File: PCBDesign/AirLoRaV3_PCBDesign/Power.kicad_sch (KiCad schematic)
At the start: 16 parts, among them J1 Barrel_Jack_Switch_Pin3Ring, U1 TPS7A2633DRVR, U4 TPS54202DDC

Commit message: Update circiut
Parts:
- added C3: 75pF, Capacitor_SMD:C_0603_1608Metric, symbol Device:C_Small
- added C5: 22uF, Capacitor_SMD:C_0603_1608Metric, symbol Device:C_Small
- added R1: 100K, Resistor_SMD:R_0603_1608Metric, symbol Device:R
- C1: value 470uF -> 10uF
- C2: renamed from C14; value 470uF -> 0.1uF; footprint Capacitor_Tantalum_SMD:CP_EIA-7343-43_Kemet-X -> Capacitor_SMD:C_0603_1608Metric
- C4: renamed from C15; value 100Uf -> 0.1uF; footprint Capacitor_Tantalum_SMD:CP_EIA-6032-15_Kemet-U -> Capacitor_SMD:C_0603_1608Metric
- C6: renamed from C2; value 100Uf -> 22uF; footprint Capacitor_Tantalum_SMD:CP_EIA-6032-15_Kemet-U -> Capacitor_SMD:C_0603_1608Metric
- C7: renamed from C3; footprint (none) -> Capacitor_SMD:C_0603_1608Metric
- C8: renamed from C5; footprint (none) -> Capacitor_SMD:C_0603_1608Metric
- L1: value 68uH -> 15uH
- R2: renamed from R7; value R -> 13.3K; footprint (none) -> Resistor_SMD:R_0603_1608Metric
- R3: renamed from R6; value R -> 49.9; footprint (none) -> Resistor_SMD:R_0603_1608Metric
- R4: renamed from R10; value R -> 10K; footprint (none) -> Resistor_SMD:R_0603_1608Metric
- R5: renamed from R8; value R -> 1.96M; footprint (none) -> Resistor_SMD:R_0603_1608Metric
- R6: renamed from R9; value R -> 1.18M; footprint (none) -> Resistor_SMD:R_0603_1608Metric
- U1: renamed from U4; LCSC (none) -> C191884; MFR (none) -> TPS54202DDCR
- U2: renamed from U1; footprint TPS7A2633DRVR:SON65P200X200X80-7N -> footprint:TPS7A2633DRVR; LCSC (none) -> C2876256; MFR (none) -> TPS7A2633DRVR
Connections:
- net GND: now also U2.7 (EXP), C5.2
- net at C4.2, L1.1, U1.2 (SW): no longer R3.1
- net at R2.1, U1.4 (FB): now also C3.2, R1.2; no longer R3.2
- net 3.3V renamed +3.3V
- net 5V renamed +5V
- net +5V: now also R3.2, C5.1
- new net: C3.1, R1.1, R3.1
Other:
- moved on the sheet: C1, C2, C4, C6, C7, C8, D1, J1, L1, R2, R3, R4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

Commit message: Update PCB layout
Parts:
- removed J1: Barrel_Jack_Switch_Pin3Ring, Connector_BarrelJack:BarrelJack_Wuerth_6941xx301002, symbol Connector:Barrel_Jack_Switch_Pin3Ring
- added D2, D3: LED, LED_SMD:LED_0603_1608Metric_Pad1.05x0.95mm_HandSolder, symbol Device:LED
- added J1: 12V, Connector_Phoenix_MC:PhoenixContact_MCV_1,5_2-G-3.5_1x02_P3.50mm_Vertical, symbol Connector:Screw_Terminal_01x02
- added R1, R5, R9: 1k, Resistor_SMD:R_0603_1608Metric, symbol Device:R
- C1: footprint Capacitor_Tantalum_SMD:CP_EIA-7343-43_Kemet-X -> Capacitor_SMD:C_1206_3216Metric_Pad1.33x1.80mm_HandSolder
- C5, C7, C8: footprint Capacitor_SMD:C_0603_1608Metric -> Capacitor_SMD:C_1206_3216Metric_Pad1.33x1.80mm_HandSolder
- L1: footprint Inductor_SMD:L_Bourns_SRP7028A_7.3x6.6mm -> Inductor_SMD:L_Vishay_IHLP-2020
- renumbered R1 to R2, R2 to R3, R3 to R4, R4 to R6, R5 to R7, R6 to R8
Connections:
- net +3.3V: now also D3.2 (A)
- net +5V: now also D2.2 (A)
- net En: now also R1.2; no longer U1.5 (EN)
- net GND: now also J1.2 (Pin_2), R5.2, R9.2
- net at D1.2 (A): now also J1.1 (Pin_1)
- net SW: now reaches C4.2, L1.1, U1.2 (SW)
- new net: D2.1 (K), R5.1
- new net: D3.1 (K), R9.1
- new net: R1.1, U1.5 (EN)

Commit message: update
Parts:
- C6: footprint Capacitor_SMD:C_0603_1608Metric -> Capacitor_SMD:C_1206_3216Metric_Pad1.33x1.80mm_HandSolder
- C7, C8: footprint Capacitor_SMD:C_1206_3216Metric_Pad1.33x1.80mm_HandSolder -> Capacitor_SMD:C_0805_2012Metric_Pad1.18x1.45mm_HandSolder

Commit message: Update schematic
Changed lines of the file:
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@@
 	(wire
 		(pts
-			(xy 57.15 87.63) (xy 57.15 80.01)
+			(xy 54.61 80.01) (xy 54.61 83.82)
 		)
 		(stroke
@@
 	(wire
 		(pts
-			(xy 54.61 80.01) (xy 57.15 80.01)
-		)
-		(stroke
-			(width 0)
-			(type default)
-		)
-	)
-	(wire
-		(pts
 			(xy 190.5 85.09) (xy 190.5 80.01)
 		)
@@
 	(wire
 		(pts
+			(xy 54.61 83.82) (xy 57.15 83.82)
+		)
+		(stroke
+			(width 0)
+			(type default)
+		)
+	)
+	(wire
+		(pts
 			(xy 121.92 87.63) (xy 125.73 87.63)
 		)
@@
 		)
 		(stroke
+			(width 0)
+			(type default)
+		)
+	)
+	(wire
+		(pts
+			(xy 57.15 83.82) (xy 57.15 87.63)
+		)
+		(stroke

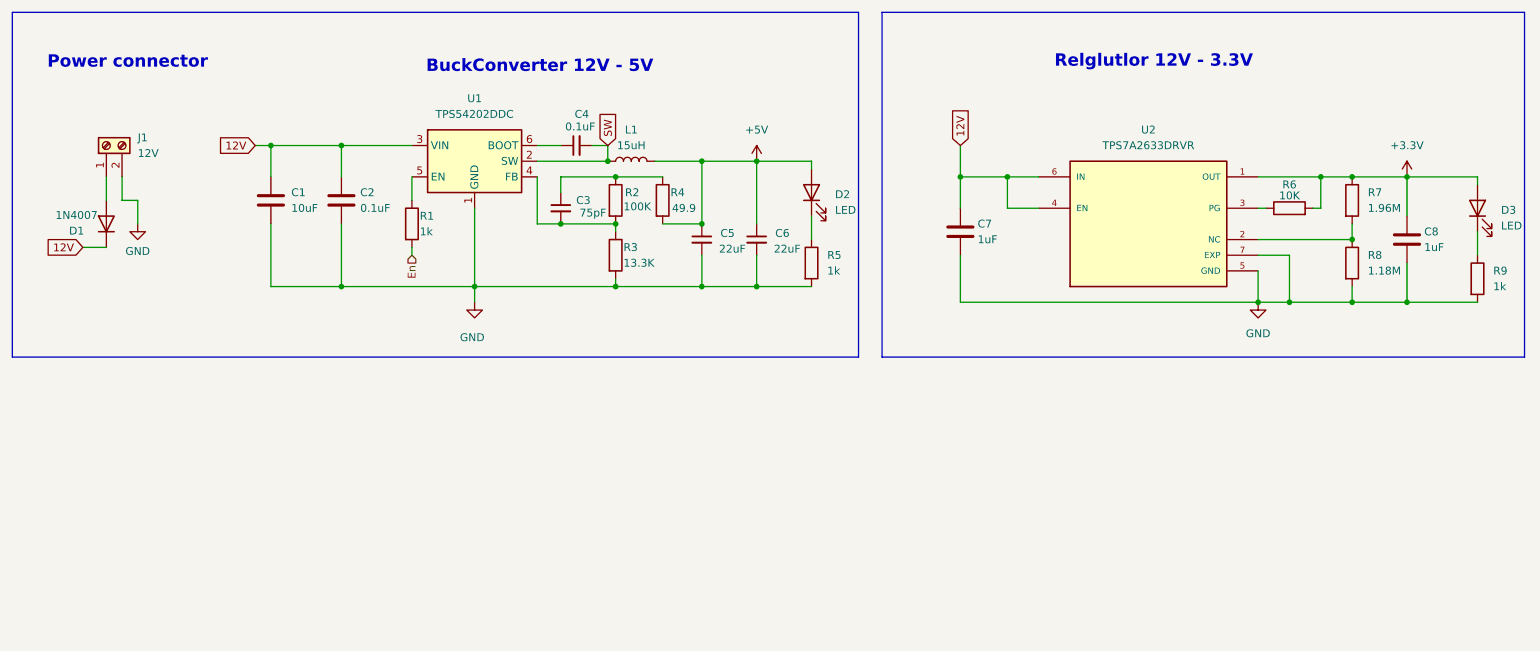
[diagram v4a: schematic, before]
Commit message: Update circuit buck converter and sensor
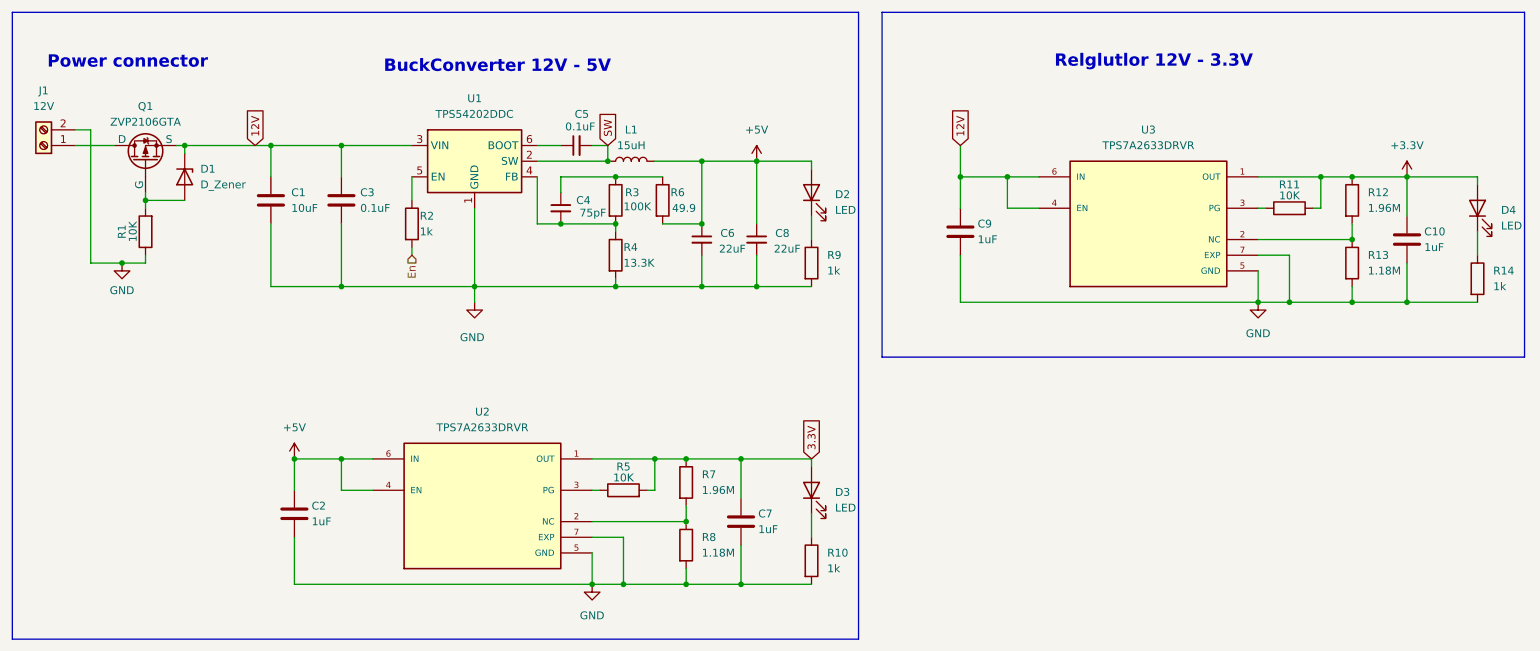
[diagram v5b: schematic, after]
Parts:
- removed D1: 1N4007, Diode_SMD:D_SMA, symbol Device:D
- added C2, C7: 1uF, Capacitor_SMD:C_0805_2012Metric_Pad1.18x1.45mm_HandSolder, symbol Device:C
- added D1: D_Zener, Diode_SMD:D_SMA_Handsoldering, symbol Device:D_Zener
- added D3: LED, LED_SMD:LED_0603_1608Metric_Pad1.05x0.95mm_HandSolder, symbol Device:LED
- added Q1: ZVP2106GTA, Package_TO_SOT_SMD:SOT-223-3_TabPin2, symbol Simulation_SPICE:PMOS
- added R1, R5: 10K, Resistor_SMD:R_0603_1608Metric, symbol Device:R
- added R10: 1k, Resistor_SMD:R_0603_1608Metric, symbol Device:R
- added R7: 1.96M, Resistor_SMD:R_0603_1608Metric, symbol Device:R
- added R8: 1.18M, Resistor_SMD:R_0603_1608Metric, symbol Device:R
- added U2: TPS7A2633DRVR, footprint:TPS7A2633DRVR, symbol TPS7A2633DRVR:TPS7A2633DRVR
- renumbered C8 to C10, C2 to C3, C3 to C4, C4 to C5, C5 to C6, C6 to C8, C7 to C9, D3 to D4, R6 to R11, R7 to R12, R8 to R13, R9 to R14, R1 to R2, R2 to R3, R3 to R4, R4 to R6, R5 to R9, U2 to U3
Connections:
- net +5V: now also C2.1, U2.4 (EN), U2.6 (IN)
- net 12V: now also D1.1 (K), Q1.3 (S)
- net GND: now also C2.2, C7.2, R1.1, R10.2, R8.2, U2.5 (GND), U2.7 (EXP)
- net at J1.1 (Pin_1): now also Q1.2 (D)
- new net: D3.1 (K), R10.1
- new net: R7.2, R8.1, U2.2 (NC)
- new net: D1.2 (A), Q1.1 (G), R1.2
- new net: R5.1, U2.3 (PG)
- new net 3.3V: C7.1, D3.2 (A), R5.2, R7.1, U2.1 (OUT)
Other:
- moved on the sheet: J1

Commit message: Update schematic
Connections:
- net 12V renamed +12V
- net 3.3V renamed +3.3V_HP
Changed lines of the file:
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@@
 	)
 	(junction
+		(at 190.5 80.01)
+		(diameter 0)
+		(color 0 0 0 0)
+	)
+	(junction
 		(at 90.17 74.93)
 		(diameter 0)
@@
 	)
 	(junction
-		(at 190.5 80.01)
+		(at 166.37 125.73)
 		(diameter 0)
 		(color 0 0 0 0)
@@
 	(wire
 		(pts
-			(xy 190.5 80.01) (xy 190.5 74.93)
-		)
-		(stroke
-			(width 0)
-			(type default)
-		)
-	)
-	(wire
-		(pts
 			(xy 101.6 83.82) (xy 101.6 80.01)
 		)
@@
 		)
 	)
-	(global_label "3.3V"
-		(shape input)
-		(at 166.37 125.73 90)
-		(fields_autoplaced yes)
-		(effects
-			(font
-				(size 1.27 1.27)
-			)
-			(justify left)
-		)
-		(property "Intersheetrefs" "${INTERSHEET_REFS}"
-			(at 166.37 118.6324 90)
-			(effects
-				(font
-					(size 1.27 1.27)
-				)
-				(justify left)
-				(hide yes)
-			)
-		)
-	)
-	(global_label "12V"
-		(shape input)
-		(at 190.5 74.93 90)
-		(fields_autoplaced yes)
-		(effects
-			(font
-				(size 1.27 1.27)
-			)
-			(justify left)
-		)
-		(property "Intersheetrefs" "${INTERSHEET_REFS}"
-			(at 190.5 68.4372 90)
-			(effects
-				(font
-					(size 1.27 1.27)
-				)
-				(justify left)
-				(hide yes)
-			)
-		)
-	)
 	(global_label "SW"
 		(shape input)
@@
 		)
 	)
-	(global_label "12V"
-		(shape input)
-		(at 76.2 74.93 90)
-		(fields_autoplaced yes)
-		(effects
-			(font
-				(size 1.27 1.27)
-			)
-			(justify left)
-		)
-		(property "Intersheetrefs" "${INTERSHEET_REFS}"
-			(at 76.2 68.4372 90)
-			(effects
-				(font
-					(size 1.27 1.27)
-				)
-				(justify left)
-				(hide yes)
-			)
-		)
-	)
 	(hierarchical_label "En"
 		(shape input)
@@
 	)
 	(symbol
+		(lib_id "power:+3.3V")
+		(at 166.37 125.73 0)
+		(unit 1)
+		(exclude_from_sim no)
+		(in_bom yes)
+		(on_board yes)
+		(dnp no)
+		(fields_autoplaced yes)
+		(property "Reference" "#PWR067"
+			(at 166.37 129.54 0)
+			(effects
+				(font
+					(size 1.27 1.27)
+				)
+				(hide yes)
+			)
+		)
+		(property "Value" "+3.3V_HP"
+			(at 166.37 120.65 0)
+			(effects
+				(font
+					(size 1.27 1.27)
+				)
+			)
+		)
+		(property "Footprint" ""
+			(at 166.37 125.73 0)
+			(effects
+				(font
+					(size 1.27 1.27)
+				)
+				(hide yes)
+			)
+		)
+		(property "Datasheet" ""
+			(at 166.37 125.73 0)
+			(effects
+				(font
+					(size 1.27 1.27)
+				)
+				(hide yes)
+			)
+		)
+		(property "Description" "Power symbol creates a global label with name \"+3.3V\""
+			(at 166.37 125.73 0)
+			(effects
+				(font
+					(size 1.27 1.27)
+				)
+				(hide yes)
+			)
+		)
+		(pin "1"
+		)
+		(instances
+			(project "airlora-kicad"
+				(path "/59d971df-d6c1-4ef7-a085-bf08b7b16047/be77b740-d58b-414b-97ce-61f1d1685314/af8bb3f5-67b6-4471-83fd-9297b14489a9"
+					(reference "#PWR067")
+					(unit 1)
+				)
+			)
+		)
+	)
+	(symbol
 		(lib_id "Device:R")
 		(at 254 83.82 0)
@@
 	)
 	(symbol
+		(lib_id "power:+12V")
+		(at 78.74 74.93 0)
+		(unit 1)
+		(exclude_from_sim no)
+		(in_bom yes)
+		(on_board yes)
+		(dnp no)
+		(fields_autoplaced yes)
+		(property "Reference" "#PWR065"
+			(at 78.74 78.74 0)
+			(effects
+				(font
+					(size 1.27 1.27)
+				)
+				(hide yes)
+			)
+		)
+		(property "Value" "+12V"
+			(at 78.74 69.85 0)
+			(effects
+				(font
+					(size 1.27 1.27)
+				)
+			)
+		)
+		(property "Footprint" ""
+			(at 78.74 74.93 0)
+			(effects
+				(font
+					(size 1.27 1.27)
+				)
+				(hide yes)
+			)
+		)
+		(property "Datasheet" ""
+			(at 78.74 74.93 0)
+			(effects
+				(font
+					(size 1.27 1.27)
+				)
+				(hide yes)
+			)
+		)
+		(property "Description" "Power symbol creates a global label with name \"+12V\""
+			(at 78.74 74.93 0)
+			(effects
+				(font
+					(size 1.27 1.27)
+				)
+				(hide yes)
+			)
+		)
+		(pin "1"
+		)
+		(instances
+			(project "airlora-kicad"
+				(path "/59d971df-d6c1-4ef7-a085-bf08b7b16047/be77b740-d58b-414b-97ce-61f1d1685314/af8bb3f5-67b6-4471-83fd-9297b14489a9"
+					(reference "#PWR065")
+					(unit 1)
+				)
+			)
+		)
+	)
+	(symbol
 		(lib_id "Device:C_Small")
 		(at 148.59 90.17 0)
@@
 					(unit 1)
 				)
+			)
+		)
+	)
+	(symbol
+		(lib_id "power:+12V")
+		(at 190.5 80.01 0)
+		(unit 1)
+		(exclude_from_sim no)
+		(in_bom yes)
+		(on_board yes)
+		(dnp no)
+		(fields_autoplaced yes)
+		(property "Reference" "#PWR066"
+			(at 190.5 83.82 0)
+			(effects
+				(font
+					(size 1.27 1.27)
+				)
+				(hide yes)
+			)
+		)
+		(property "Value" "+12V"
+			(at 190.5 74.93 0)
+			(effects
+				(font
+					(size 1.27 1.27)
+				)
+			)
+		)
+		(property "Footprint" ""
+			(at 190.5 80.01 0)
+			(effects
+				(font
+					(size 1.27 1.27)
+				)
+				(hide yes)
+			)
+		)
+		(property "Datasheet" ""
+			(at 190.5 80.01 0)
+			(effects
+				(font
+					(size 1.27 1.27)
+				)
+				(hide yes)
+			)
+		)
+		(property "Description" "Power symbol creates a global label with name \"+12V\""
+			(at 190.5 80.01 0)
+			(effects
+				(font
+					(size 1.27 1.27)
+				)
+				(hide yes)
+			)
+		)
+		(pin "1"
+		)
+		(instances
+			(project "airlora-kicad"
+				(path "/59d971df-d6c1-4ef7-a085-bf08b7b16047/be77b740-d58b-414b-97ce-61f1d1685314/af8bb3f5-67b6-4471-83fd-9297b14489a9"
+					(reference "#PWR066")
+					(unit 1)
+				)
